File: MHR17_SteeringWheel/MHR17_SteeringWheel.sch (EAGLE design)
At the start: 0 parts

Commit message: add CAN transiever
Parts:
- added IC1: AT90CAN128, at90can128:AT90CAN128
- added U$1: MCP2551-I/SN, Microchip_By_element14_Batch_1:MCP2551-I/SN
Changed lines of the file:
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@@
 <grid distance="0.1" unitdist="inch" unit="inch" style="lines" multiple="1" display="no" altdistance="0.01" altunitdist="inch" altunit="inch"/>
 <layers>
+<layer number="1" name="Top" color="4" fill="1" visible="no" active="no"/>
+<layer number="16" name="Bottom" color="1" fill="1" visible="no" active="no"/>
+<layer number="17" name="Pads" color="2" fill="1" visible="no" active="no"/>
+<layer number="18" name="Vias" color="2" fill="1" visible="no" active="no"/>
+<layer number="19" name="Unrouted" color="6" fill="1" visible="no" active="no"/>
+<layer number="20" name="Dimension" color="15" fill="1" visible="no" active="no"/>
+<layer number="21" name="tPlace" color="7" fill="1" visible="no" active="no"/>
+<layer number="22" name="bPlace" color="7" fill="1" visible="no" active="no"/>
+<layer number="23" name="tOrigins" color="15" fill="1" visible="no" active="no"/>
+<layer number="24" name="bOrigins" color="15" fill="1" visible="no" active="no"/>
+<layer number="25" name="tNames" color="7" fill="1" visible="no" active="no"/>
+<layer number="26" name="bNames" color="7" fill="1" visible="no" active="no"/>
+<layer number="27" name="tValues" color="7" fill="1" visible="no" active="no"/>
+<layer number="28" name="bValues" color="7" fill="1" visible="no" active="no"/>
+<layer number="29" name="tStop" color="7" fill="3" visible="no" active="no"/>
+<layer number="30" name="bStop" color="7" fill="6" visible="no" active="no"/>
+<layer number="31" name="tCream" color="7" fill="4" visible="no" active="no"/>
+<layer number="32" name="bCream" color="7" fill="5" visible="no" active="no"/>
+<layer number="33" name="tFinish" color="6" fill="3" visible="no" active="no"/>
+<layer number="34" name="bFinish" color="6" fill="6" visible="no" active="no"/>
+<layer number="35" name="tGlue" color="7" fill="4" visible="no" active="no"/>
+<layer number="36" name="bGlue" color="7" fill="5" visible="no" active="no"/>
+<layer number="37" name="tTest" color="7" fill="1" visible="no" active="no"/>
+<layer number="38" name="bTest" color="7" fill="1" visible="no" active="no"/>
+<layer number="39" name="tKeepout" color="4" fill="11" visible="no" active="no"/>
+<layer number="40" name="bKeepout" color="1" fill="11" visible="no" active="no"/>
+<layer number="41" name="tRestrict" color="4" fill="10" visible="no" active="no"/>
+<layer number="42" name="bRestrict" color="1" fill="10" visible="no" active="no"/>
+<layer number="43" name="vRestrict" color="2" fill="10" visible="no" active="no"/>
+<layer number="44" name="Drills" color="7" fill="1" visible="no" active="no"/>
+<layer number="45" name="Holes" color="7" fill="1" visible="no" active="no"/>
+<layer number="46" name="Milling" color="3" fill="1" visible="no" active="no"/>
+<layer number="47" name="Measures" color="7" fill="1" visible="no" active="no"/>
+<layer number="48" name="Document" color="7" fill="1" visible="no" active="no"/>
+<layer number="49" name="Reference" color="7" fill="1" visible="no" active="no"/>
+<layer number="51" name="tDocu" color="7" fill="1" visible="no" active="no"/>
+<layer number="52" name="bDocu" color="7" fill="1" visible="no" active="no"/>
 <layer number="90" name="Modules" color="5" fill="1" visible="yes" active="yes"/>
 <layer number="91" name="Nets" color="2" fill="1" visible="yes" active="yes"/>
@@
 </classes>
 <parts>
+<part name="IC1" library="at90can128" deviceset="AT90CAN128" device=""/>
+<part name="U$1" library="Microchip_By_element14_Batch_1" deviceset="MCP2551-I/SN" device=""/>
 </parts>
 <sheets>
@@
 </plain>
 <instances>
+<instance part="IC1" gate="G$1" x="50.8" y="58.42"/>
+<instance part="U$1" gate="A" x="139.7" y="114.3"/>
 </instances>
 <busses>

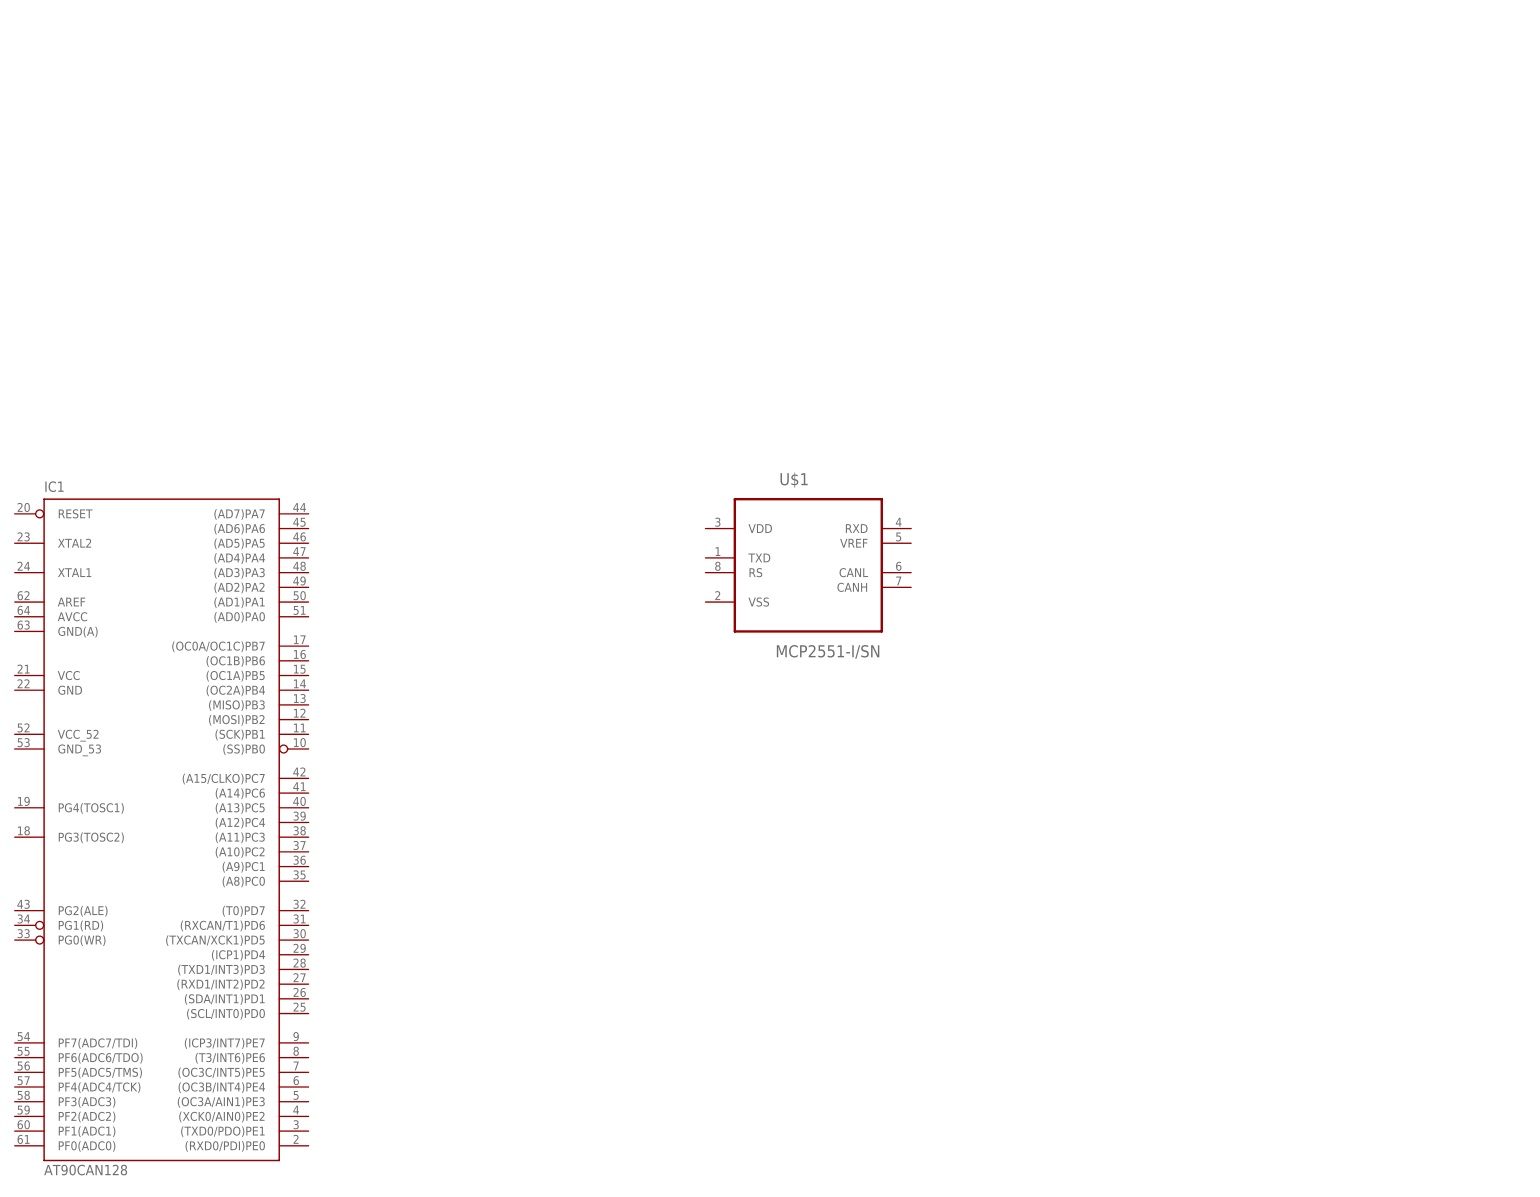
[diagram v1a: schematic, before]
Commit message: added output ports, still need to check wiresize
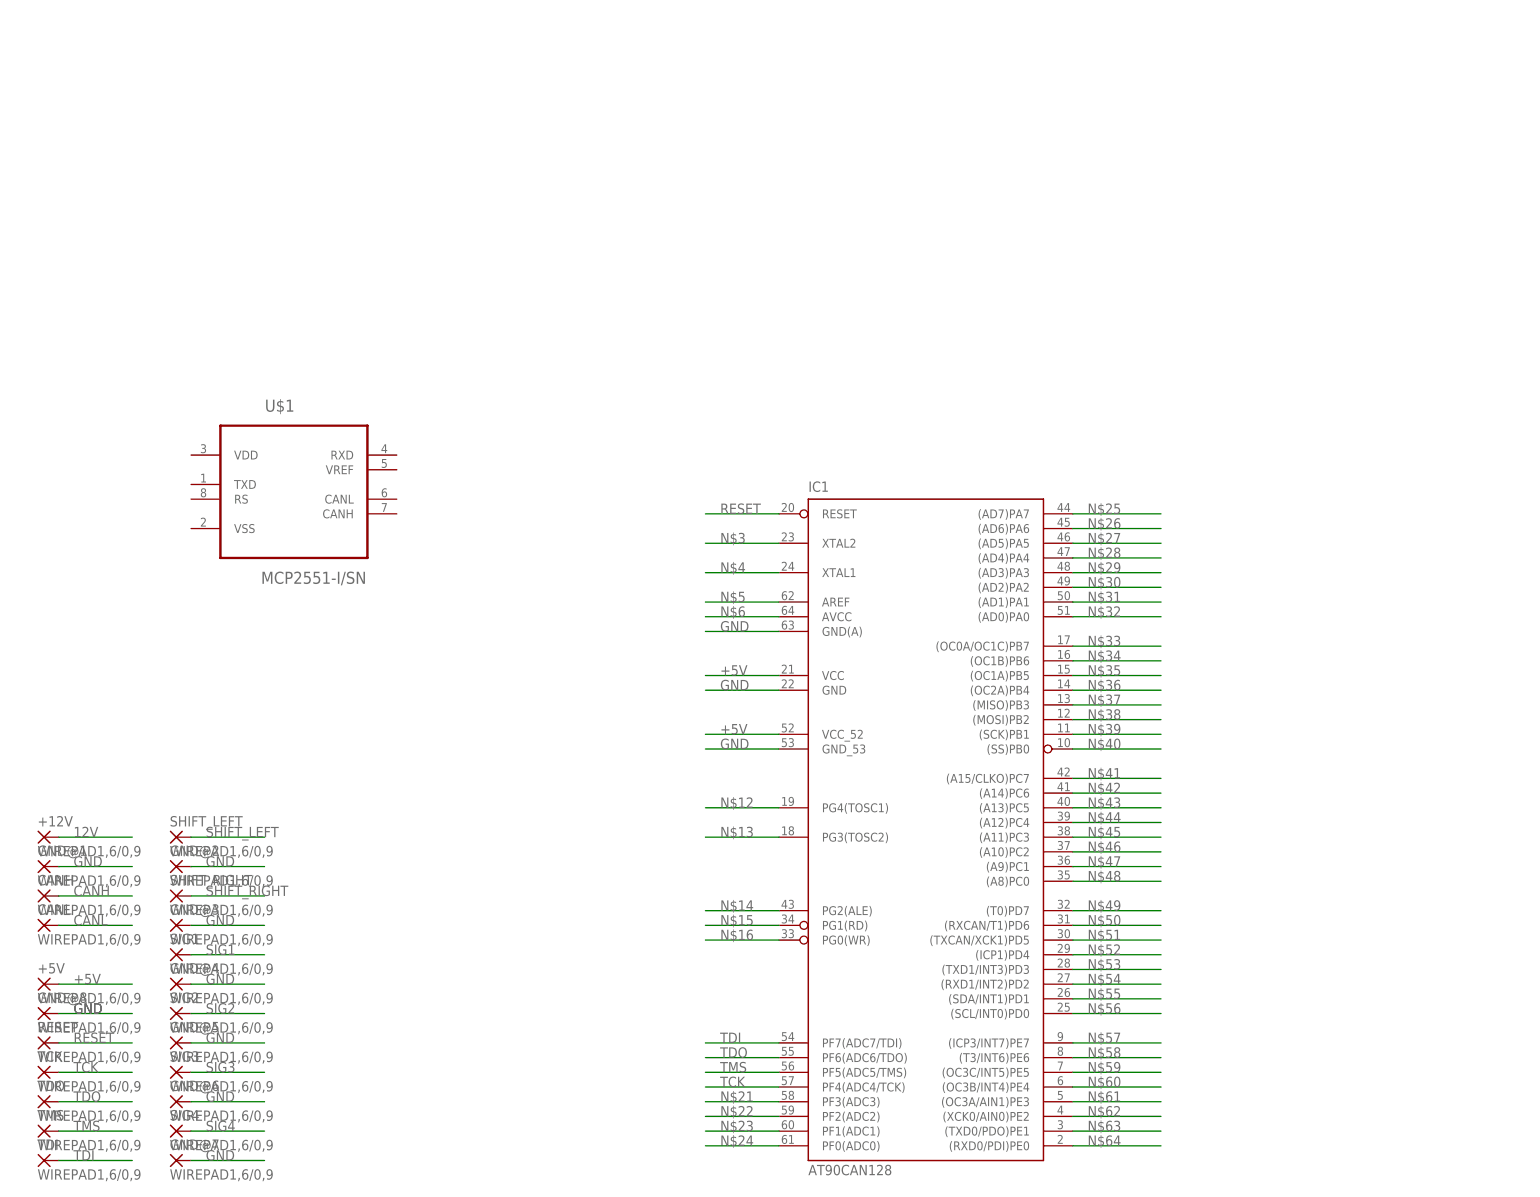
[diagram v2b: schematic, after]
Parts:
- added +12V, +5V, CANH, CANL, GND@1, GND@2, GND@3, GND@4, GND@5, GND@6, GND@7, GND@8, RESET, SHIFT_LEFT, SHIFT_RIGHT, SIG1, SIG2, SIG3, SIG4, TCK, TDI, TDO, TMS: WIREPAD1,6/0,9, wirepad:WIREPAD1,6/0,9
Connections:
- new net +5V: +5V.P, IC1.VCC, IC1.VCC_52
- new net 12V: +12V.P
- new net CANH: CANH.P
- new net CANL: CANL.P
- new net GND: GND@1.P, GND@2.P, GND@3.P, GND@4.P, GND@5.P, GND@6.P, GND@7.P, GND@8.P, IC1.GND, IC1.GND(A), IC1.GND_53
- new net N$12: IC1.PG4(TOSC1)
- new net N$13: IC1.PG3(TOSC2)
- new net N$14: IC1.PG2(ALE)
- new net N$15: IC1.PG1(RD)
- new net N$16: IC1.PG0(WR)
- new net N$21: IC1.PF3(ADC3)
- new net N$22: IC1.PF2(ADC2)
- new net N$23: IC1.PF1(ADC1)
- new net N$24: IC1.PF0(ADC0)
- new net N$25: IC1.(AD7)PA7
- new net N$26: IC1.(AD6)PA6
- new net N$27: IC1.(AD5)PA5
- new net N$28: IC1.(AD4)PA4
- new net N$29: IC1.(AD3)PA3
- new net N$3: IC1.XTAL2
- new net N$30: IC1.(AD2)PA2
- new net N$31: IC1.(AD1)PA1
- new net N$32: IC1.(AD0)PA0
- new net N$33: IC1.(OC0A/OC1C)PB7
- new net N$34: IC1.(OC1B)PB6
- new net N$35: IC1.(OC1A)PB5
- new net N$36: IC1.(OC2A)PB4
- new net N$37: IC1.(MISO)PB3
- new net N$38: IC1.(MOSI)PB2
- new net N$39: IC1.(SCK)PB1
- new net N$4: IC1.XTAL1
- new net N$40: IC1.(SS)PB0
- new net N$41: IC1.(A15/CLKO)PC7
- new net N$42: IC1.(A14)PC6
- new net N$43: IC1.(A13)PC5
- new net N$44: IC1.(A12)PC4
- new net N$45: IC1.(A11)PC3
- new net N$46: IC1.(A10)PC2
- new net N$47: IC1.(A9)PC1
- new net N$48: IC1.(A8)PC0
- new net N$49: IC1.(T0)PD7
- new net N$5: IC1.AREF
- new net N$50: IC1.(RXCAN/T1)PD6
- new net N$51: IC1.(TXCAN/XCK1)PD5
- new net N$52: IC1.(ICP1)PD4
- new net N$53: IC1.(TXD1/INT3)PD3
- new net N$54: IC1.(RXD1/INT2)PD2
- new net N$55: IC1.(SDA/INT1)PD1
- new net N$56: IC1.(SCL/INT0)PD0
- new net N$57: IC1.(ICP3/INT7)PE7
- new net N$58: IC1.(T3/INT6)PE6
- new net N$59: IC1.(OC3C/INT5)PE5
- new net N$6: IC1.AVCC
- new net N$60: IC1.(OC3B/INT4)PE4
- new net N$61: IC1.(OC3A/AIN1)PE3
- new net N$62: IC1.(XCK0/AIN0)PE2
- new net N$63: IC1.(TXD0/PDO)PE1
- new net N$64: IC1.(RXD0/PDI)PE0
- new net RESET: IC1.RESET, RESET.P
- new net SHIFT_LEFT: SHIFT_LEFT.P
- new net SHIFT_RIGHT: SHIFT_RIGHT.P
- new net SIG1: SIG1.P
- new net SIG2: SIG2.P
- new net SIG3: SIG3.P
- new net SIG4: SIG4.P
- new net TCK: IC1.PF4(ADC4/TCK), TCK.P
- new net TDI: IC1.PF7(ADC7/TDI), TDI.P
- new net TDO: IC1.PF6(ADC6/TDO), TDO.P
- new net TMS: IC1.PF5(ADC5/TMS), TMS.P
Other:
- moved on the sheet: IC1, U$1

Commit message: added frame for schematic
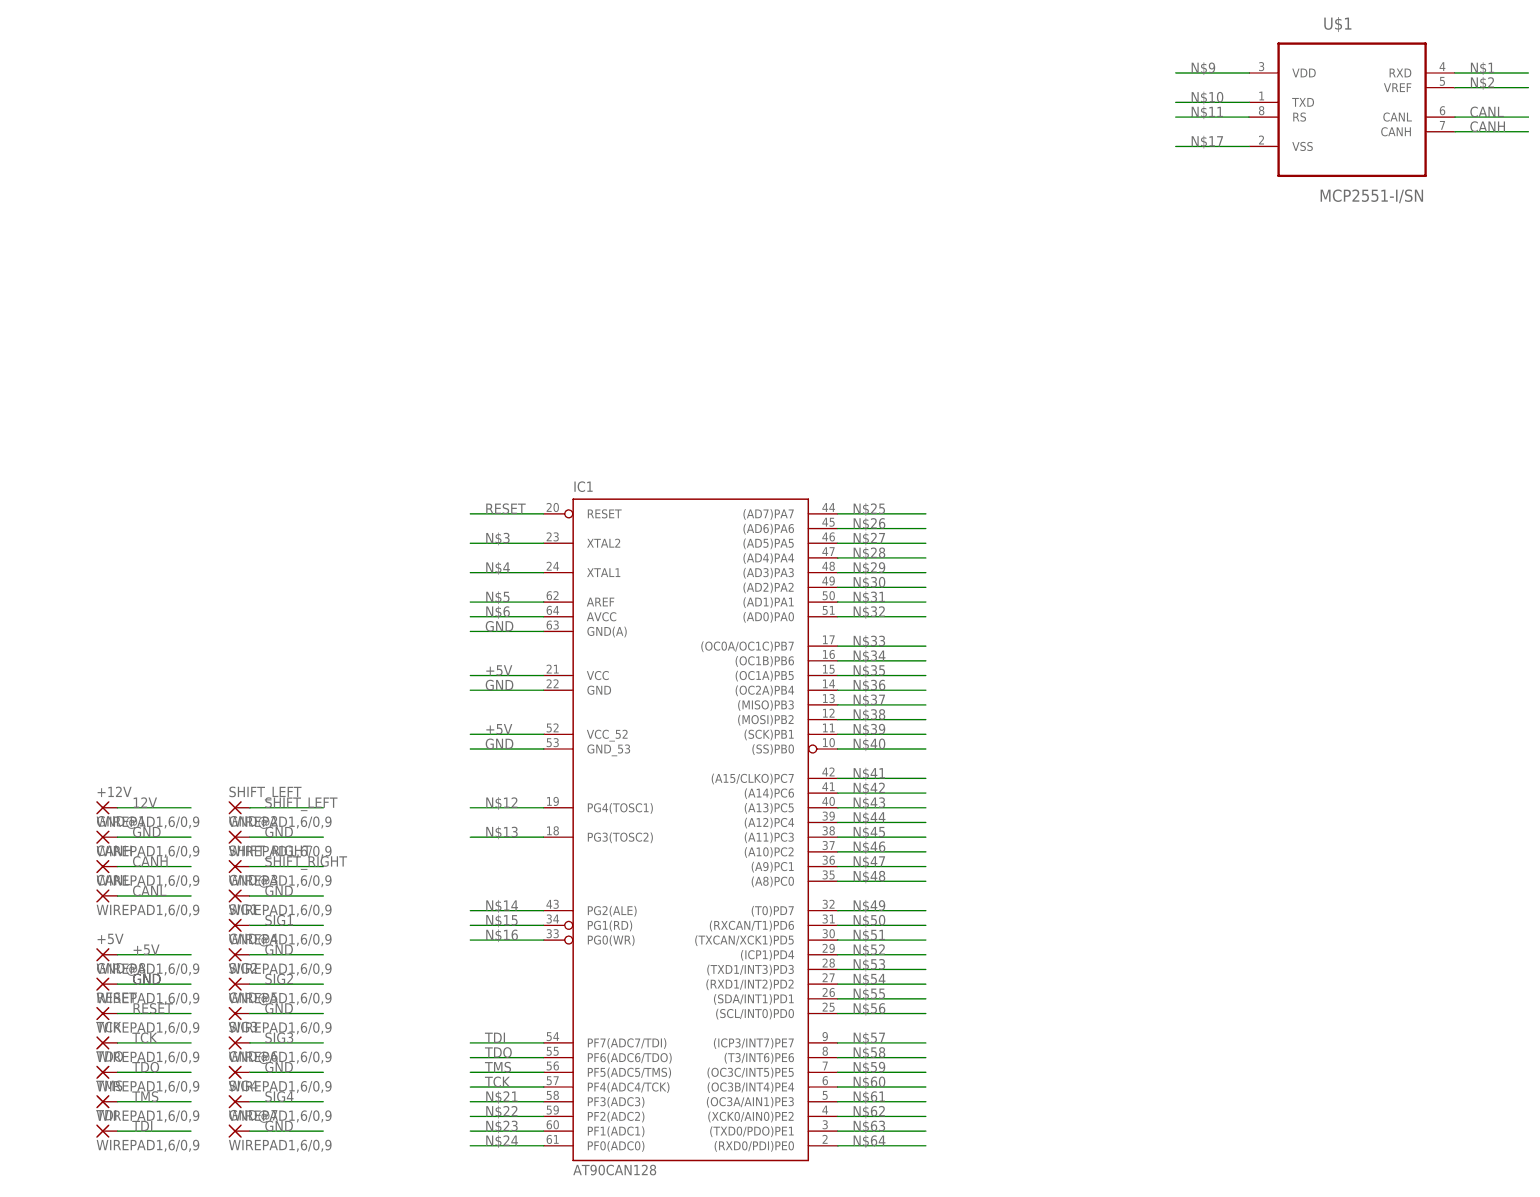
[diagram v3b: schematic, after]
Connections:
- new net N$1: U$1.RXD
- new net N$10: U$1.TXD
- new net N$11: U$1.RS
- new net N$17: U$1.VSS
- new net N$2: U$1.VREF
- new net N$9: U$1.VDD
- net CANH: now also U$1.CANH
- net CANL: now also U$1.CANL
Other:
- moved on the sheet: +12V, +5V, CANH, CANL, GND@1, GND@2, GND@3, GND@4, GND@5, GND@6, GND@7, GND@8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

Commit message: changed dimensions and added power for various ports
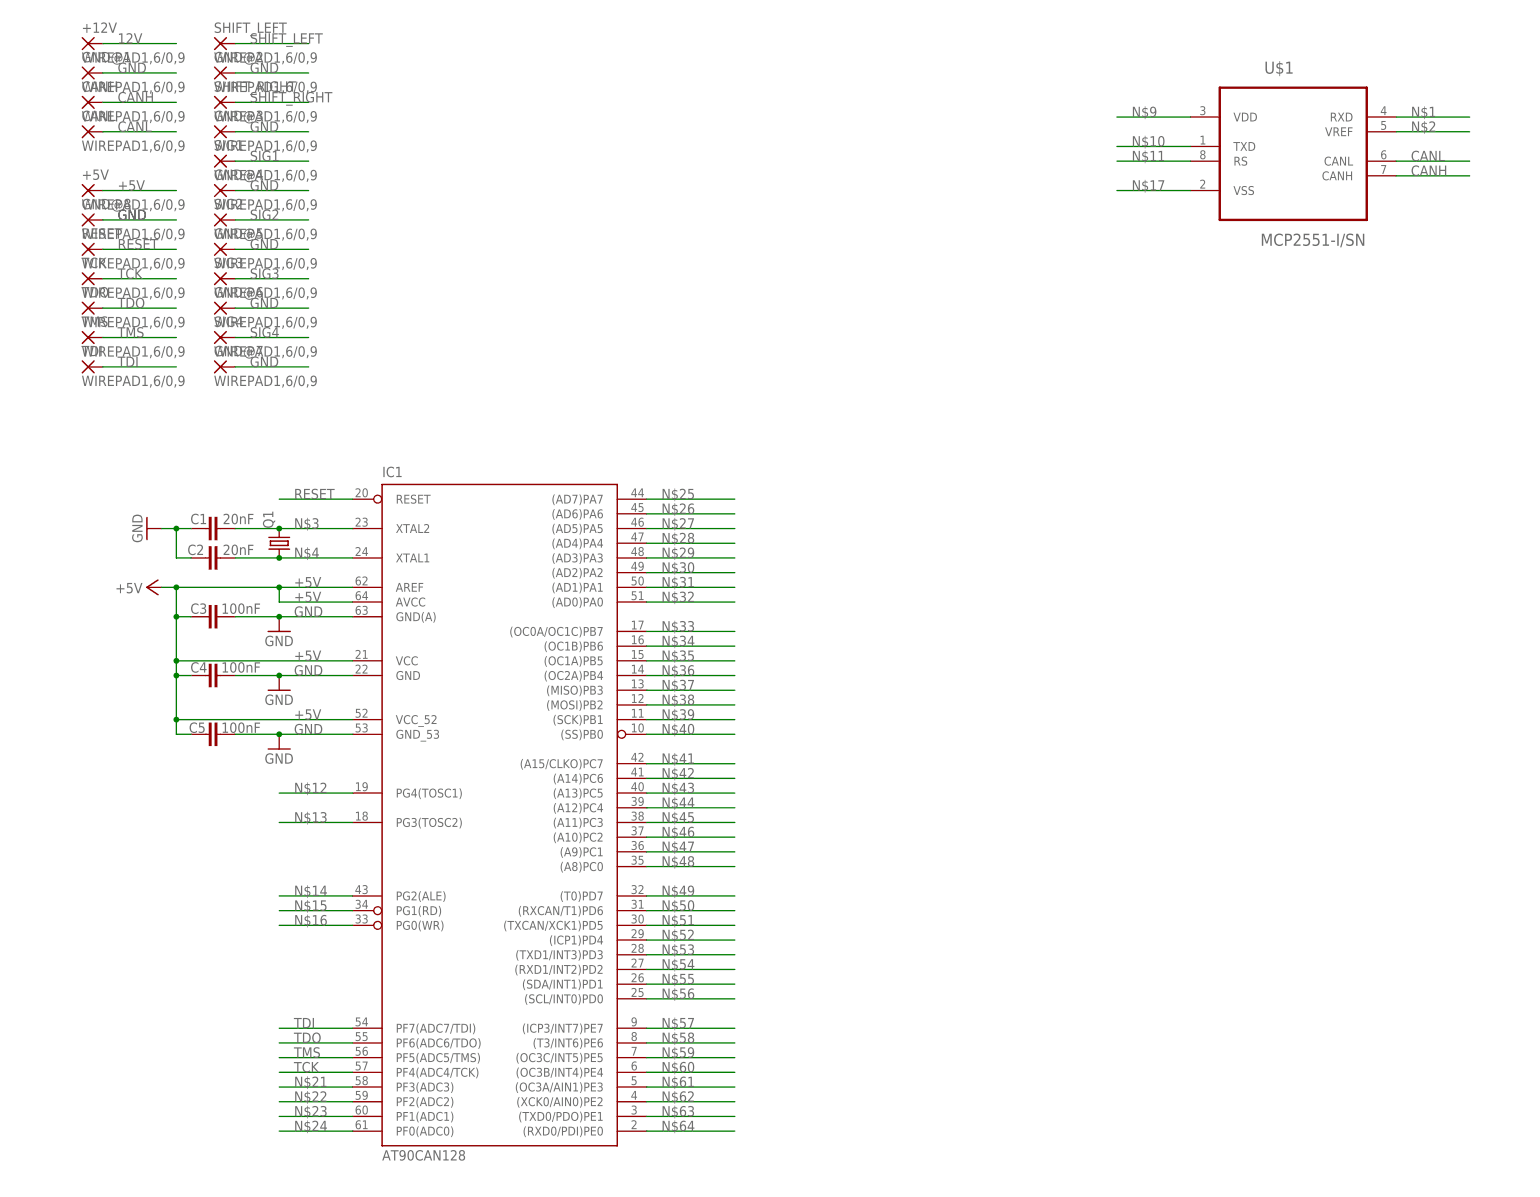
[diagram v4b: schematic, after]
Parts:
- added C1, C2: 20nF, rcl:C-EUC0603
- added C3, C4, C5: 100nF, rcl:C-EUC0603
- added Q1: (no value), crystal:CRYSTALHC49S
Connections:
- removed net N$5: IC1.AREF
- removed net N$6: IC1.AVCC
- net +5V: now also C3.1, C4.1, C5.1, IC1.AREF, IC1.AVCC
- net GND: now also C1.1, C2.1, C3.2, C4.2, C5.2
- net N$3: now also C1.2, Q1.2
- net N$4: now also C2.2, Q1.1
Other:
- moved on the sheet: +12V, +5V, CANH, CANL, GND@1, GND@2, GND@3, GND@4, GND@5, GND@6, GND@7, GND@8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
